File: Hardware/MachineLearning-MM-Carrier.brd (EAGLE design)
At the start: 58.4 x 52.1 mm, 125 parts, among them J11 microSD, J2 JTAG, J3 QWIIC_RIGHT_ANGLE, J4 MICROMOD-2222-C, J7 CAMERA-HIMAX, U3 AP2127K-1.8V, U4 LIS2DH12, U5 AP7361C-33FGE

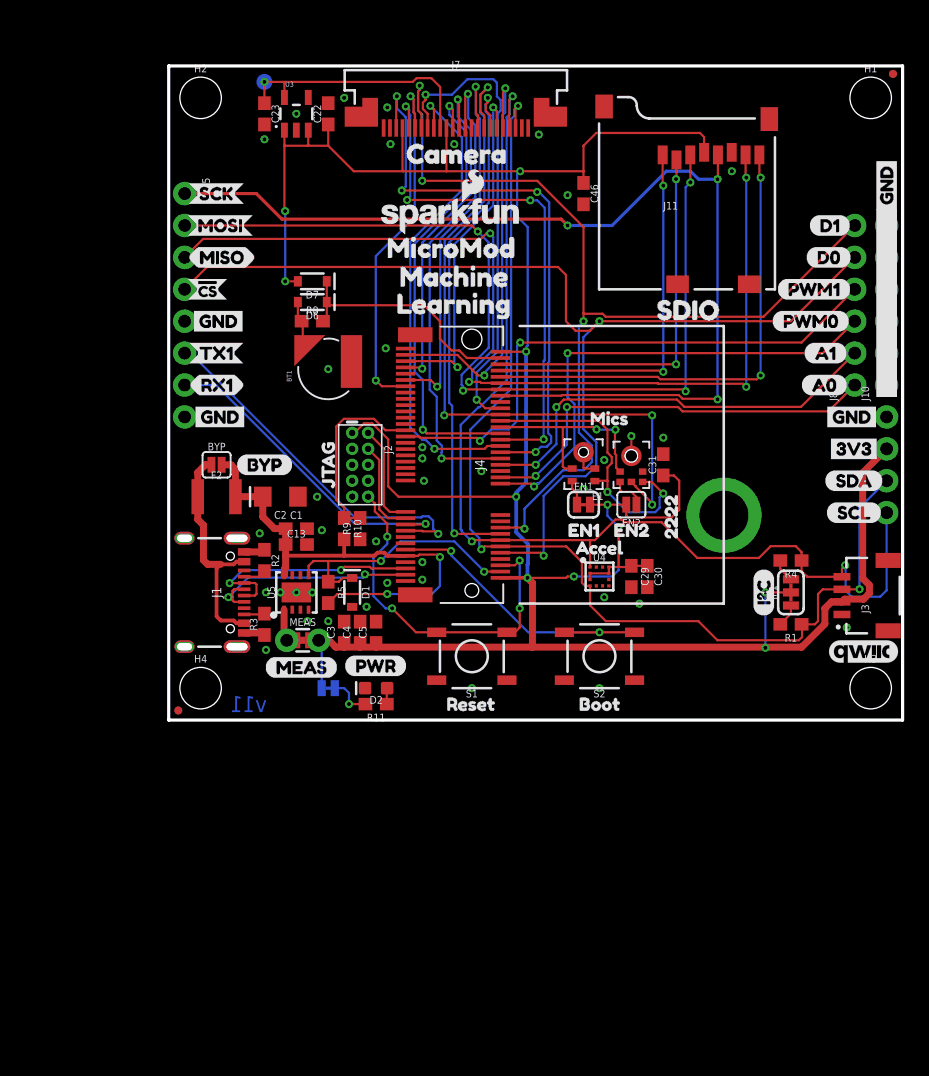
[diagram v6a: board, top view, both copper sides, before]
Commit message: Re-route camera connector for face up. Convert buzzard labels. Add power control to camera regulator.
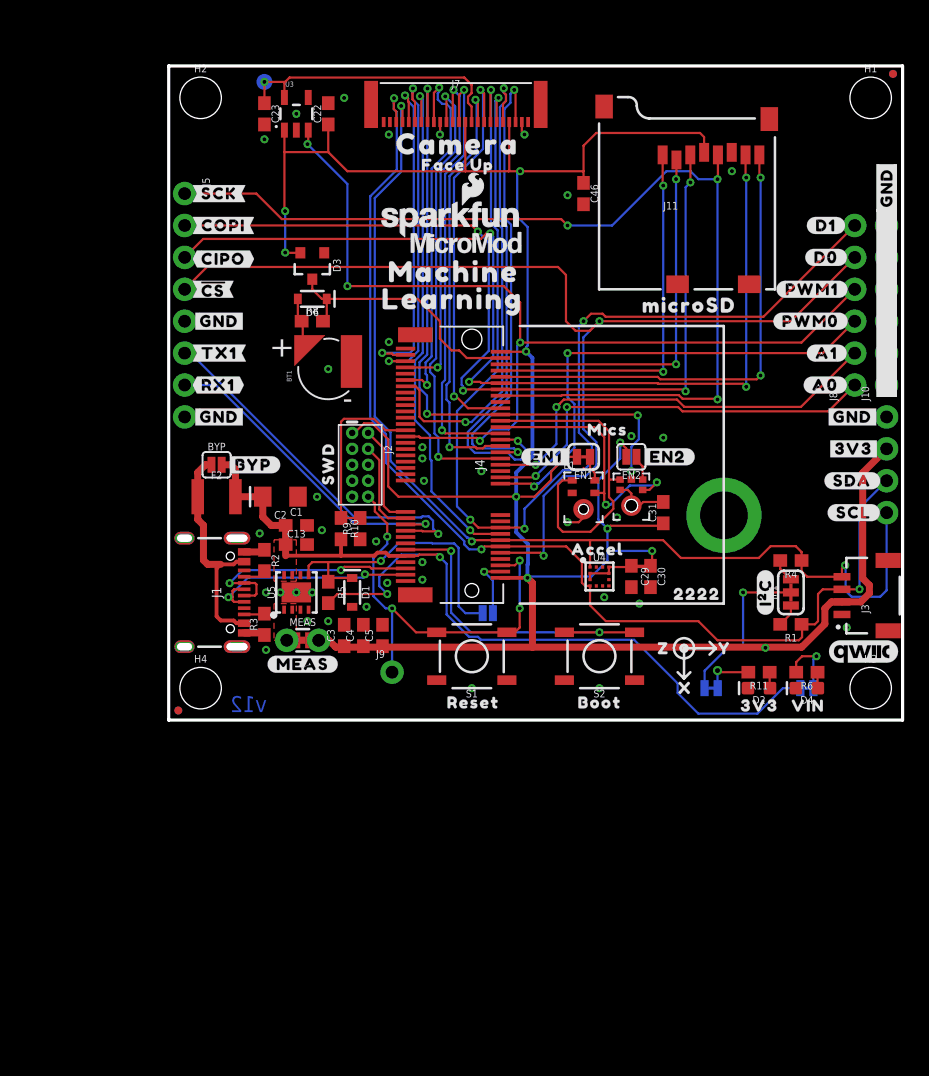
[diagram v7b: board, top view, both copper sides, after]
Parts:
- removed D7: 1A/23V/620mV, SparkFun-DiscreteSemi:SOD-323
- removed JP4: (no value), SparkFun-Jumpers:SMT-JUMPER_2_NC_TRACE_SILK
- removed U$53, U$54: (no value), SparkFun-Buzzard:GND_P
- removed U$55: (no value), buzzard_labels (9):22229
- removed U$57, U$58: (no value), buzzard_labels (1):A10
- removed U$59, U$60: (no value), buzzard_labels (1):PWM01
- removed U$61: (no value), buzzard_labels (10):PWM10
- removed U$64: (no value), buzzard_labels (11):MICROMOD0
- removed U$65: (no value), buzzard_labels (11):MACHINE2
- removed U$66: (no value), buzzard_labels (11):LEARNING3
- added 3V3_LED, VIN_LED: (no value), SparkFun-Jumpers:SMT-JUMPER_2_NC_TRACE_SILK
- added D3: BAS70-05, SparkFun-DiscreteSemi:SOT23-3
- added D4: Yellow, SparkFun-LED:LED-0603
- added J9: (no value), SparkFun-Connectors:1X01_NO_SILK
- added R6: 4.7k, SparkFun-Resistors:0603
- added U$23: (no value), output:#I�C#0
- added U$28: (no value), output:MICROSD0
- added U$30: (no value), output:LEARNING1
- added U$33: (no value), output:#BYP#1
- added U$68: (no value), output:##CS##3
- added U$69, U$70: (no value), output:#CIPO#2
- added U$71, U$72: (no value), output:#COPI#1
- added U$73, U$74, U$81, U$82: (no value), output:#GND#4
- added U$75, U$76: (no value), output:#RX1#6
- added U$77, U$78: (no value), output:#SCK#0
- added U$79, U$80: (no value), output:#TX1#5
- added VE: (no value), SparkFun-Jumpers:SMT-JUMPER_2_NO_SILK
- J5: value (none) -> SPI
- J6: value (none) -> UART
- J7: value CAMERA-HIMAX -> CAMERA-HIMAXFACEUP; device SparkFun-Connectors:FPC-24-AMPHENOL-SFV24R-1STE1HLF -> SparkFun-Connectors:FPC05024-42201
- J8: value (none) -> Dedicated
- U$1: device buzzard_labels (11):ACCEL6 -> output:#EN1#3
- U$10: device SparkFun-Buzzard:!CS_O -> output:#D0#1
- U$11: device SparkFun-Buzzard:GND_P -> output:#GND#0
- U$12: device buzzard_labels (12):D13 -> output:#GND#0
- U$13: device buzzard_labels (12):D13 -> output:#3V3#1
- U$14: device buzzard_labels (12):D02 -> output:#3V3#1
- U$15: device buzzard_labels (10):PWM10 -> output:#GND#0
- U$16: device buzzard_labels (12):D02 -> output:#GND#0
- U$17: device SparkFun-Buzzard:PWR -> output:#RST#1
- U$18: device SparkFun-Buzzard:JTAG_TO -> output:#VE#0
- U$19: device buzzard_labels (10):BOOT2 -> output:#MEAS#2
- U$2: device buzzard_labels (9):RESET3 -> output:#EN2#4
- U$20: device SparkFun-Buzzard:PWR_TO -> output:#VIN#1
- U$21: device buzzard_labels (10):SDIO1 -> output:SWD0
- U$22: device buzzard_labels (11):MACHINE2 -> output:FACE_UP0
- U$24: device buzzard_labels (11):MICROMOD0 -> SparkFun-MicroMod:MICROMOD_LOGO_.35
- U$25: device buzzard_labels (6):RX10 -> output:#D0#1
- U$26: device buzzard_labels (12):MICS0 -> output:MACHINE0
- U$27: device SparkFun-Buzzard:BYP -> output:LEARNING1
- U$29: device buzzard_labels (6):RX10 -> output:#D1#0
- U$3: device buzzard_labels (11):CAMERA5 -> output:CAMERA0
- U$31: device buzzard_labels (6):TX13 -> output:#D1#0
- U$32: device SparkFun-Buzzard:GND_P -> output:#PWM0#3
- U$34: device buzzard_labels (7):EN13 -> SparkFun-MicroMod:MICROMOD_LOGO_.35
- U$35: device buzzard_labels (7):EN24 -> output:##CS##3
- U$36: device SparkFun-Buzzard:GND_P -> output:3V37
- U$37: device SparkFun-Buzzard:I2C -> output:MACHINE0
- U$38: device SparkFun-Buzzard:3V3_P -> output:22223
- U$39: device SparkFun-Buzzard:SDA_IO -> output:ACCEL4
- U$4: device buzzard_labels (11):LEARNING3 -> output:#3V3#0
- U$40: device SparkFun-Buzzard:SCL_IO -> output:BOOT5
- U$41: device buzzard_labels (6):TX13 -> output:#PWM0#3
- U$42: device SparkFun-Buzzard:GND_P -> output:#PWM1#2
- U$43, U$44: device buzzard_labels (12):A00 -> output:#SCL#3
- U$45: device SparkFun-Buzzard:GND_P -> output:RESET6
- U$46: device SparkFun-Buzzard:3V3_P -> output:VIN8
- U$47: device SparkFun-Buzzard:SDA_IO -> output:X1
- U$48: device SparkFun-Buzzard:SCL_IO -> output:Y2
- U$49: device SparkFun-Buzzard:SCK_O -> output:#PWM1#2
- U$5: device SparkFun-Buzzard:MEAS -> output:MICS0
- U$50: device SparkFun-Buzzard:MOSI_O -> output:#SDA#2
- U$51: device SparkFun-Buzzard:MISO_I -> output:#SDA#2
- U$52: device SparkFun-Buzzard:!CS_O -> output:Z0
- U$6: device SparkFun-Buzzard:GND_P -> output:#A0#5
- U$7: device SparkFun-Buzzard:MOSI_O -> output:#A0#5
- U$8: device SparkFun-Buzzard:MISO_I -> output:#A1#4
- U$9: device SparkFun-Buzzard:SCK_O -> output:#A1#4
- moved U$7 54.1 mm to (54.0, 26.7), flipped to the bottom
- moved U$9 54.0 mm to (54.0, 29.2), flipped to the bottom
- moved U$51 52.9 mm to (56.6, 19.1)
- moved U$10 52.8 mm to (54.0, 36.8), flipped to the bottom
- moved U$41 52.6 mm to (54.1, 31.8), flipped to the bottom
- moved U$25 50.1 mm to (50.7, 36.8)
- moved U$8 49.9 mm to (50.8, 29.2)
- moved U$50 49.7 mm to (52.2, 19.1), flipped to the top
- moved U$6 49.3 mm to (50.5, 26.7)
- moved U$31 48.8 mm to (53.8, 39.4)
- moved U$49 48.5 mm to (54.0, 34.3)
- moved U$42 47.8 mm to (48.4, 34.3)
- moved U$29 46.6 mm to (50.8, 39.4), flipped to the top
- moved LOGO3 44.5 mm to (7.62, 48.3)
- moved U$52 43.9 mm to (38.2, 5.71), flipped to the top
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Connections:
- net HEADER_!CS! renamed D0/HEADER_!CS!
- net N$1 renamed VREG_3.3V
- removed net PWM1: J4.47, J8.4
- removed net SD_!CS!: J11.CS, J4.70
- removed net SD_DAT1: J11.RSV2, J4.66
- removed net SD_DAT2: J11.RSV1, J4.68
- removed net SPI_MISO: J11.DO, J4.64, J5.3
- removed net SPI_MOSI: J11.DI, J4.62, J5.2
- new net N$1: R6.2, VIN_LED.1
- new net N$12: D1.C, R5.1, U5.5, VE.2
- new net N$8: D4.A, R6.1
- new net PWM1/CAM_VDD: J4.47, J8.4, U3.3
- new net SDIO_DAT1: J11.DAT1, J4.66
- new net SDIO_DAT2: J11.DAT2, J4.68
- new net SPI_!CS!/SDIO_DAT3: J11.CS/DAT3, J4.70
- new net SPI_SDI: J11.DO/DAT0, J4.64, J5.3
- new net SPI_SDO: J11.DI/CMD, J4.62, J5.2
- net !RESET!: now also J9.1
- net 1.8V: now also J7.15; no longer J7.10
- net 3.3V: now also 3V3_LED.2, D3.2, J7.14, J7.21; no longer D7.A, J7.11, J7.4, JP4.2, U3.3
- net 3.3V_EN: now also VE.1; no longer D1.C, R5.1, U5.5
- net CAMERA_D0: now also J7.11; no longer J7.14
- net CAMERA_D1: now also J7.22; no longer J7.3
- net CAMERA_D2: now also J7.16; no longer J7.9
- net CAMERA_D3: now also J7.20; no longer J7.5
- net CAMERA_D4: now also J7.13; no longer J7.12
- net CAMERA_D5: now also J7.5; no longer J7.20
- net CAMERA_D6: now also J7.6; no longer J7.19
- net CAMERA_D7: now also J7.12; no longer J7.13
- net CAMERA_HSYNC: now also J7.9; no longer J7.16
- net CAMERA_INT: now also J7.7; no longer J7.18
- net CAMERA_MCLK: now also J7.17; no longer J7.8
- net CAMERA_VSYNC: now also J7.19; no longer J7.6
- net D1/CAMERA_TRIG: now also J7.18; no longer J7.7
- net GND: now also D4.C, J7.10, J7.23; no longer J7.15, J7.2
- net I2C_SCL: now also J7.4; no longer J7.21
- net I2C_SDA: now also J7.3; no longer J7.22
- net I2S_SD/CAMERA_PCLK: now also J7.8; no longer J7.17
- net N$6: now also 3V3_LED.1; no longer JP4.1
- net RTC_3V: now also D3.3; no longer D7.C
- net VIN: now also VIN_LED.2
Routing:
- net SPI_SDI: track 0.00 -> 78.5 mm, vias 0 -> 4
- net SPI_MISO: track 78.5 -> 0.00 mm, vias 4 -> 0
- net PWM1/CAM_VDD: track 0.00 -> 75.6 mm, vias 0 -> 4
- net SPI_SDO: track 0.00 -> 74.3 mm, vias 0 -> 4
- net SPI_MOSI: track 74.3 -> 0.00 mm, vias 4 -> 0
- net PWM1: track 44.4 -> 0.00 mm, vias 2 -> 0
- net SD_DAT1: track 38.5 -> 0.00 mm, vias 2 -> 0
- net SDIO_DAT1: track 0.00 -> 38.5 mm, vias 0 -> 2
- net VIN: track 38.8 -> 75.4 mm
- net SD_DAT2: track 30.3 -> 0.00 mm, vias 2 -> 0
- net SDIO_DAT2: track 0.00 -> 30.3 mm, vias 0 -> 2
- net SPI_!CS!/SDIO_DAT3: track 0.00 -> 30.3 mm, vias 0 -> 2
- net SD_!CS!: track 30.3 -> 0.00 mm, vias 2 -> 0
- net N$12: track 0.00 -> 24.0 mm, vias 0 -> 1
- net 3.3V_EN: track 21.5 -> 4.89 mm, vias 2 -> 1
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- added copper zone on layer 1, net VIN
- added copper zone on layer 1, net VREG_3.3V
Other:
- board text added: "+"
- board text added: "-"
- board text added: "N. Seidle"
- board text added: "v12"
- board text removed: "v11"

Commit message: Update MicroMod connector with SPI port changes
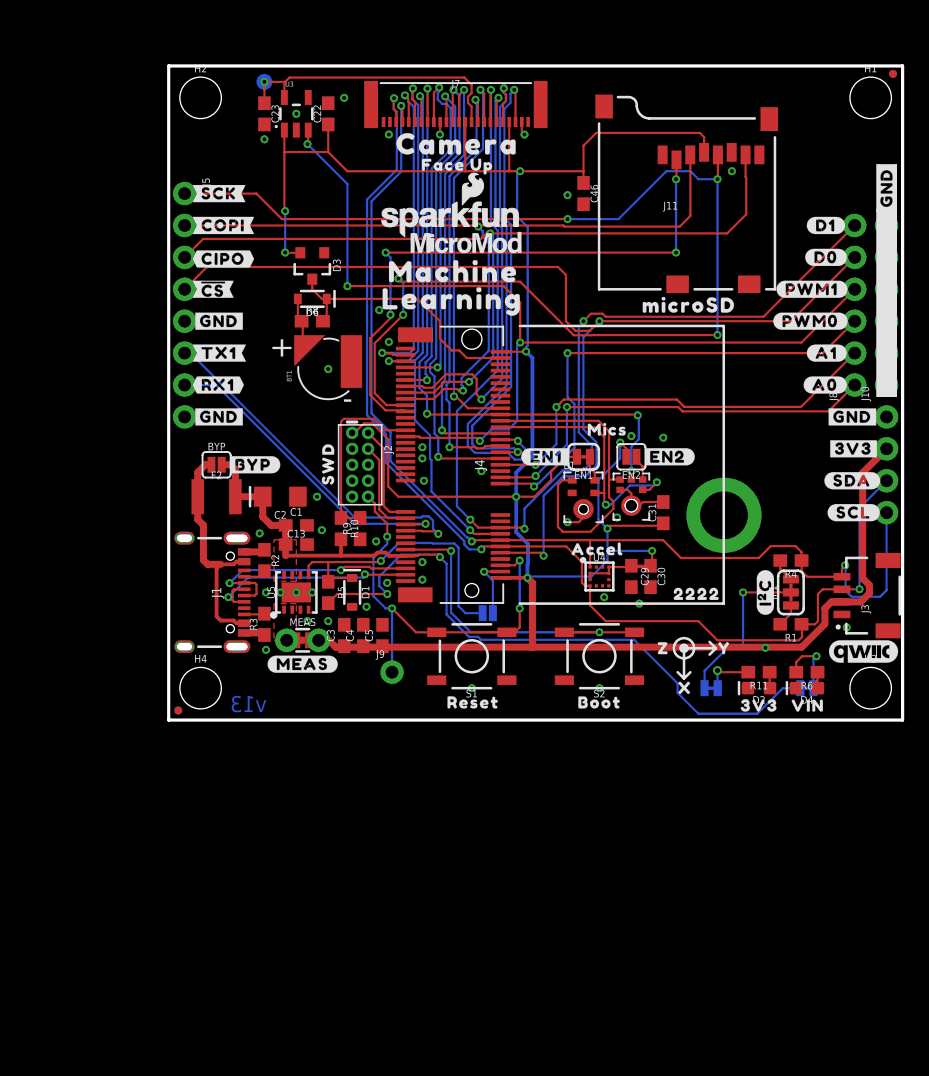
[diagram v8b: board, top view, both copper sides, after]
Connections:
- removed net SDIO_DAT1: J11.DAT1, J4.66
- removed net SDIO_DAT2: J11.DAT2, J4.68
- removed net SPI_!CS!/SDIO_DAT3: J11.CS/DAT3, J4.70
- new net SPI_!CS!: J11.CS/DAT3, J4.55
- net SPI_SCK: now also J4.57; no longer J4.60
- net SPI_SDI: now also J4.61; no longer J4.64
- net SPI_SDO: now also J4.59; no longer J4.62
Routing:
- net SPI_!CS!: track 0.00 -> 46.0 mm, vias 0 -> 4
- net SDIO_DAT1: track 38.5 -> 0.00 mm, vias 2 -> 0
- net SDIO_DAT2: track 30.3 -> 0.00 mm, vias 2 -> 0
- net SPI_!CS!/SDIO_DAT3: track 30.3 -> 0.00 mm, vias 2 -> 0
- net SPI_SCK: track 82.4 -> 99.8 mm, vias 3 -> 5
- net SPI_SDI: track 78.5 -> 69.0 mm, vias 4 -> 2
- net SPI_SDO: track 74.3 -> 64.9 mm, vias 4 -> 2
- net CAMERA_VSYNC: track 36.8 -> 35.1 mm
- net CAMERA_HSYNC: track 30.0 -> 29.5 mm
- net GND: vias 38 -> 39
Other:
- board text added: "v13"
- board text removed: "v12"
